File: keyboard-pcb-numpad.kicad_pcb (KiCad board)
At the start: 2 copper layers, 37 parts, among them SW1 SW_Push, U1 ProMicro

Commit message: feat: complete route
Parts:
- D1, D10, D11, D12, D13, D14, D15, D16, D17, D2, D3, D4, D5, D6, D7, D8, D9: moved to B.Cu
- moved D2 203.5 mm to (56.9, 81.5), turned to 90 degrees
- moved D4 198.0 mm to (57.0, 119.5), turned to 90 degrees
- moved D3 193.6 mm to (56.8, 100.5), turned to 90 degrees
- moved D8 188.4 mm to (76.0, 119.5), turned to 90 degrees
- moved D1 182.4 mm to (56.8, 62.4), turned to 90 degrees
- moved D7 179.5 mm to (75.9, 100.5), turned to 90 degrees
- moved D6 177.4 mm to (75.9, 81.5), turned to 90 degrees
- moved D9 173.0 mm to (66.4, 138.6), turned to 90 degrees
- moved D12 164.3 mm to (94.9, 100.5), turned to 90 degrees
- moved D5 163.4 mm to (75.9, 62.4), turned to 90 degrees
- moved D10 161.6 mm to (94.9, 62.4), turned to 90 degrees
- moved D14 150.9 mm to (94.9, 138.6), turned to 90 degrees
- moved D17 149.8 mm to (114.0, 129.1), turned to 90 degrees
- moved D16 147.0 mm to (114.0, 91.0), turned to 90 degrees
- moved D11 146.5 mm to (94.9, 81.5), turned to 90 degrees
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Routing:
- net ROW2: track 0.00 -> 331.7 mm
- net COL1: track 0.00 -> 266.1 mm
- net ROW1: track 0.00 -> 262.8 mm
- net COL2: track 0.00 -> 182.9 mm
- net COL0: track 0.00 -> 181.7 mm
- net ROW0: track 0.00 -> 127.8 mm
- net ROW3: track 0.00 -> 125.0 mm
- net ROW4: track 0.00 -> 110.1 mm
- net COL3: track 0.00 -> 106.2 mm
- net GND: track 0.00 -> 99.1 mm
- net /RST: track 0.00 -> 84.9 mm
- net +5V: track 0.00 -> 41.0 mm
- net Net-(D4-Pad2): track 0.00 -> 12.5 mm
- net Net-(D8-Pad2): track 0.00 -> 12.5 mm
- net Net-(D13-Pad2): track 0.00 -> 12.5 mm
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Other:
- board outline added: 100 x 99 mm
- net class Default: trace_width 0.25 -> 0.254
- net class Power added: clearance 0.2, trace_width 0.381, via_dia 0.8, via_drill 0.4

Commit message: fix: fix route
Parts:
- turned R1 to 180 degrees
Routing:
- net ROW2: track 331.7 -> 86.6 mm
- net ROW1: track 262.8 -> 70.1 mm
- net COL1: track 266.1 -> 165.8 mm
- net ROW0: track 127.8 -> 63.9 mm
- net COL2: track 182.9 -> 141.2 mm
- net ROW3: track 125.0 -> 97.3 mm
- net COL0: track 181.7 -> 161.0 mm
- net COL3: track 106.2 -> 111.5 mm
- net GND: track 99.1 -> 98.1 mm

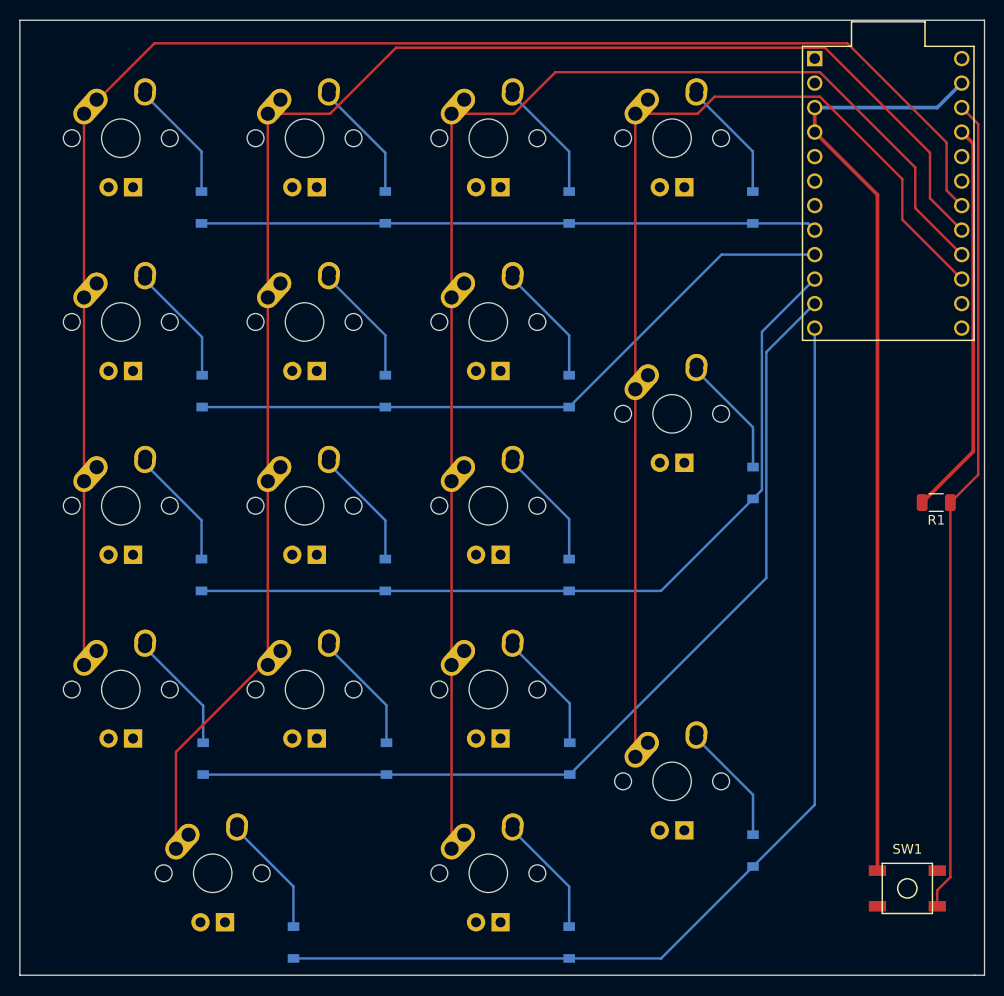
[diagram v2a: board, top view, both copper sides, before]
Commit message: feat: fill ground
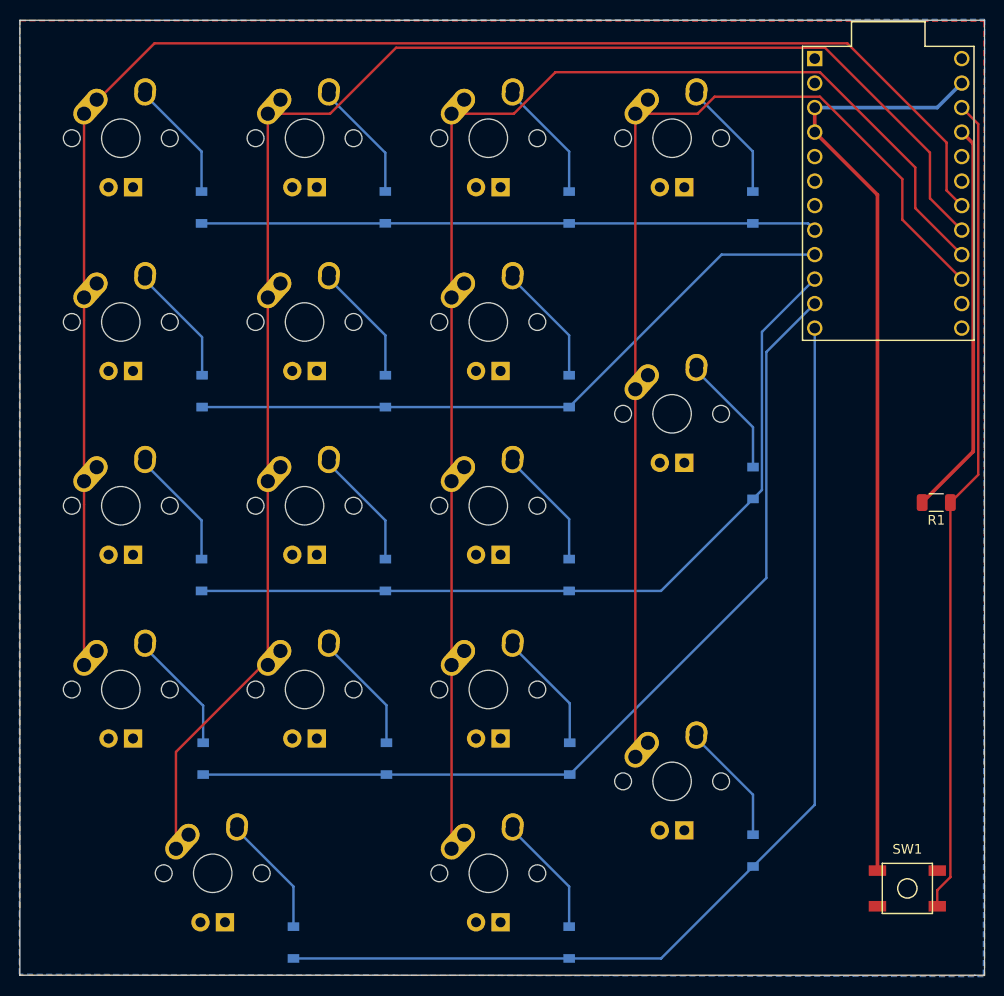
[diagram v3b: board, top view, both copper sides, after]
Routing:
- added copper zone on B.Cu, net GND
- added copper zone on F.Cu, net GND
